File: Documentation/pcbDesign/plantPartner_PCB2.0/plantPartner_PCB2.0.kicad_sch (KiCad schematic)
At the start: 67 parts, among them IC1 MPM3610, J1 Conn_01x04, J10 Screw_Terminal_01x02, J11 Conn_01x02, J12 Conn_01x03, J13 Conn_01x03, J14 Conn_01x03, J16 Conn_01x04, J17 Conn_01x03, J2 Conn_01x04, J20 Conn_02x04_Top_Bottom, J21 Conn_01x04, J22 Conn_01x04, J23 Conn_01x01, J24 Conn_01x03, J25 Conn_01x03, J26 Conn_01x01, J27 Conn_01x01, J28 Conn_01x01, J29 Conn_01x02, J3 Conn_01x04, J30 Screw_Terminal_01x02, J4 Screw_Terminal, J5 Conn_01x02, J6 Barrel_Jack, J7 Screw_Terminal_01x02, J8 Conn_02x04_Top_Bottom, J9 Screw_Terminal_01x02, Q1 AO3400A, Q2 AO3400A, Q4 AO3400A, U2 MAX485, U3 ESP32-DEVKIT-V1

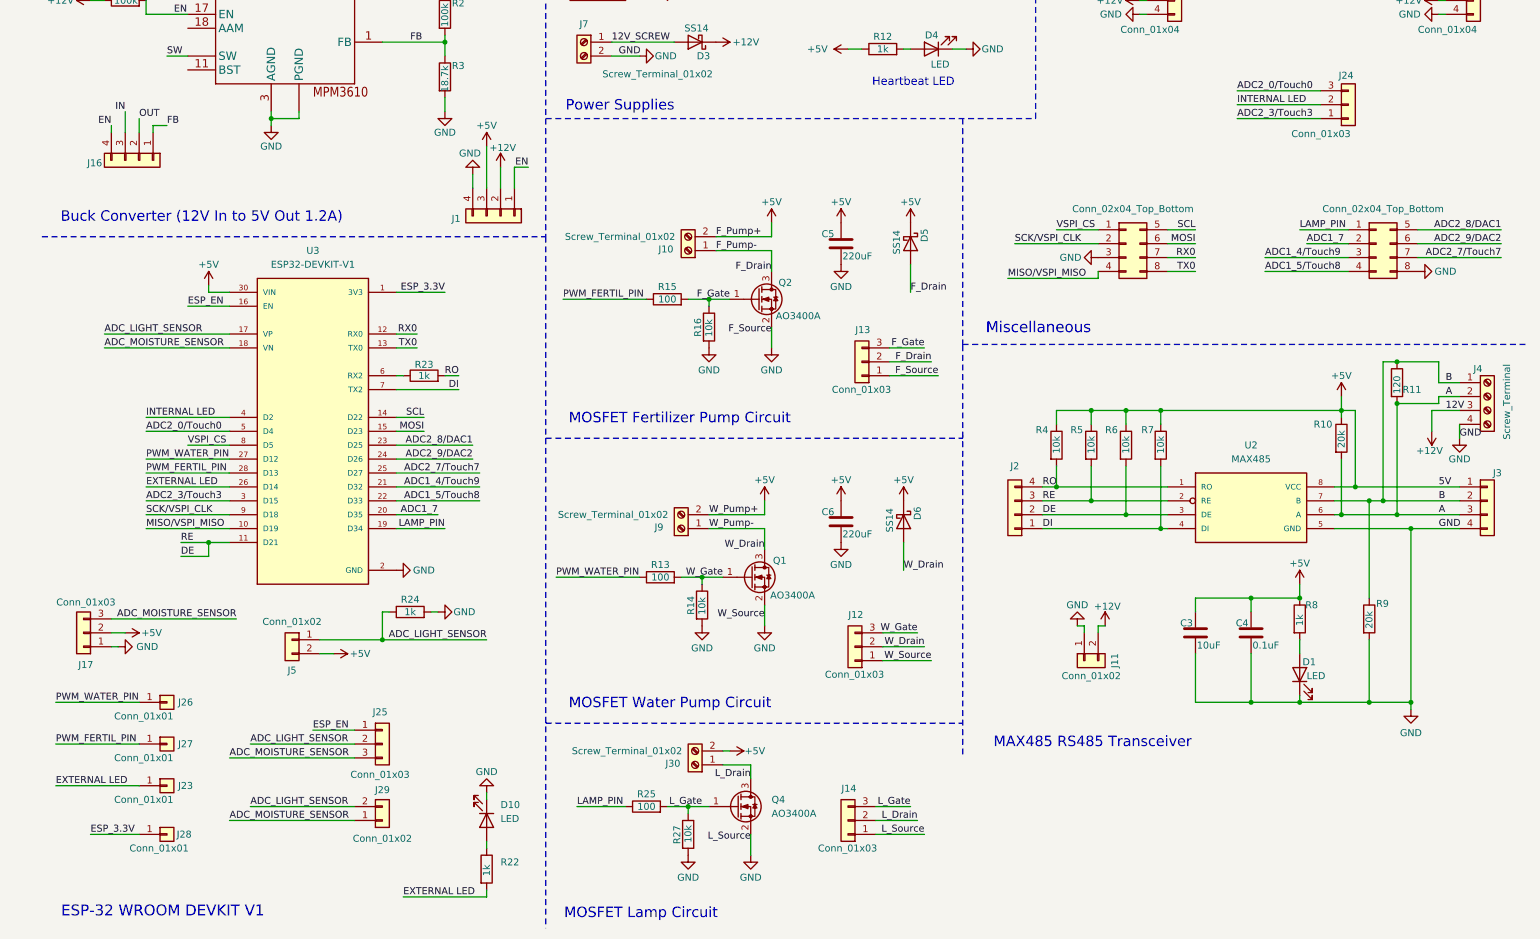
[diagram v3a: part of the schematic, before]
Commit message: Routed v2 PCB some more. Finished routing power sources, Buck Converter, MOSFET circuits, and most of RS485 Transceiver. I forgot about KiCad but will not next time I get a big chunk of time
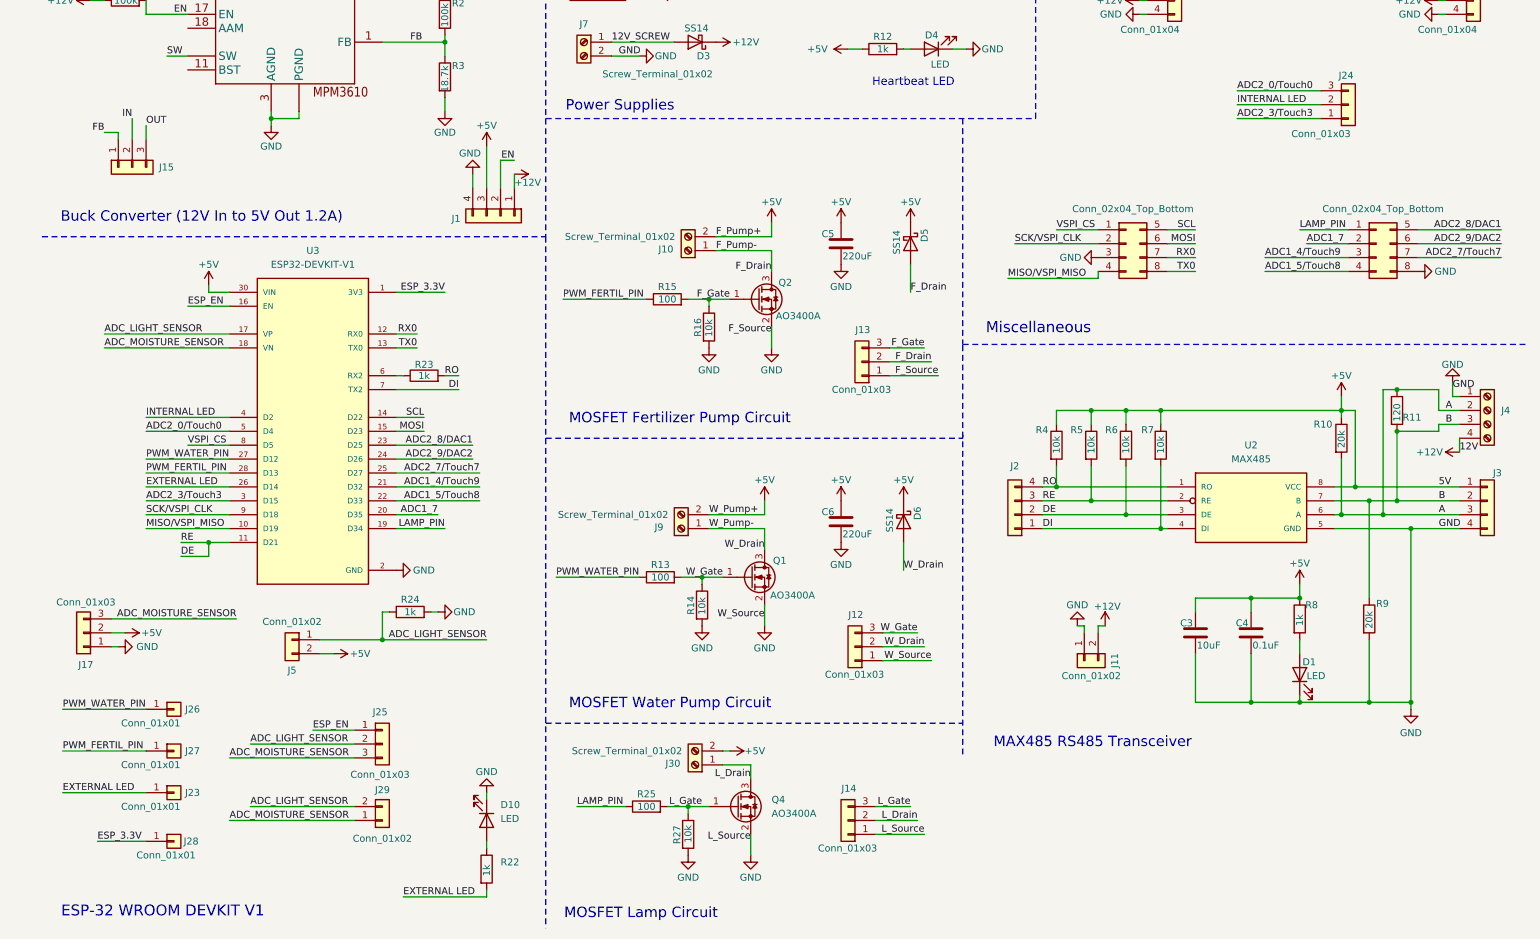
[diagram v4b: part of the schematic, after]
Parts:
- removed J16: Conn_01x04, Connector_PinHeader_2.54mm:PinHeader_1x04_P2.54mm_Vertical, symbol Connector_Generic:Conn_01x04
- added J15: Conn_01x03, Connector_PinHeader_2.54mm:PinHeader_1x03_P2.54mm_Vertical, symbol Connector_Generic:Conn_01x03
- J4: value Screw_Terminal -> Screw_Terminal_01x04
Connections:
- net +12V: now also J1.1 (Pin_1), J4.4 (Pin_4), J15.2 (Pin_2); no longer J1.2 (Pin_2), J4.3 (Pin_3)
- net +5V: now also J15.3 (Pin_3)
- net A: now also R11.1; no longer R11.2
- net B: now also J4.3 (Pin_3), R11.2; no longer J4.1 (Pin_1), R11.1
- net EN: now also J1.2 (Pin_2); no longer J1.1 (Pin_1)
- net FB: now also J15.1 (Pin_1)
- net GND: now also J4.1 (Pin_1); no longer J4.4 (Pin_4)
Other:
- moved on the sheet: J23, J26, J27, J28, R11

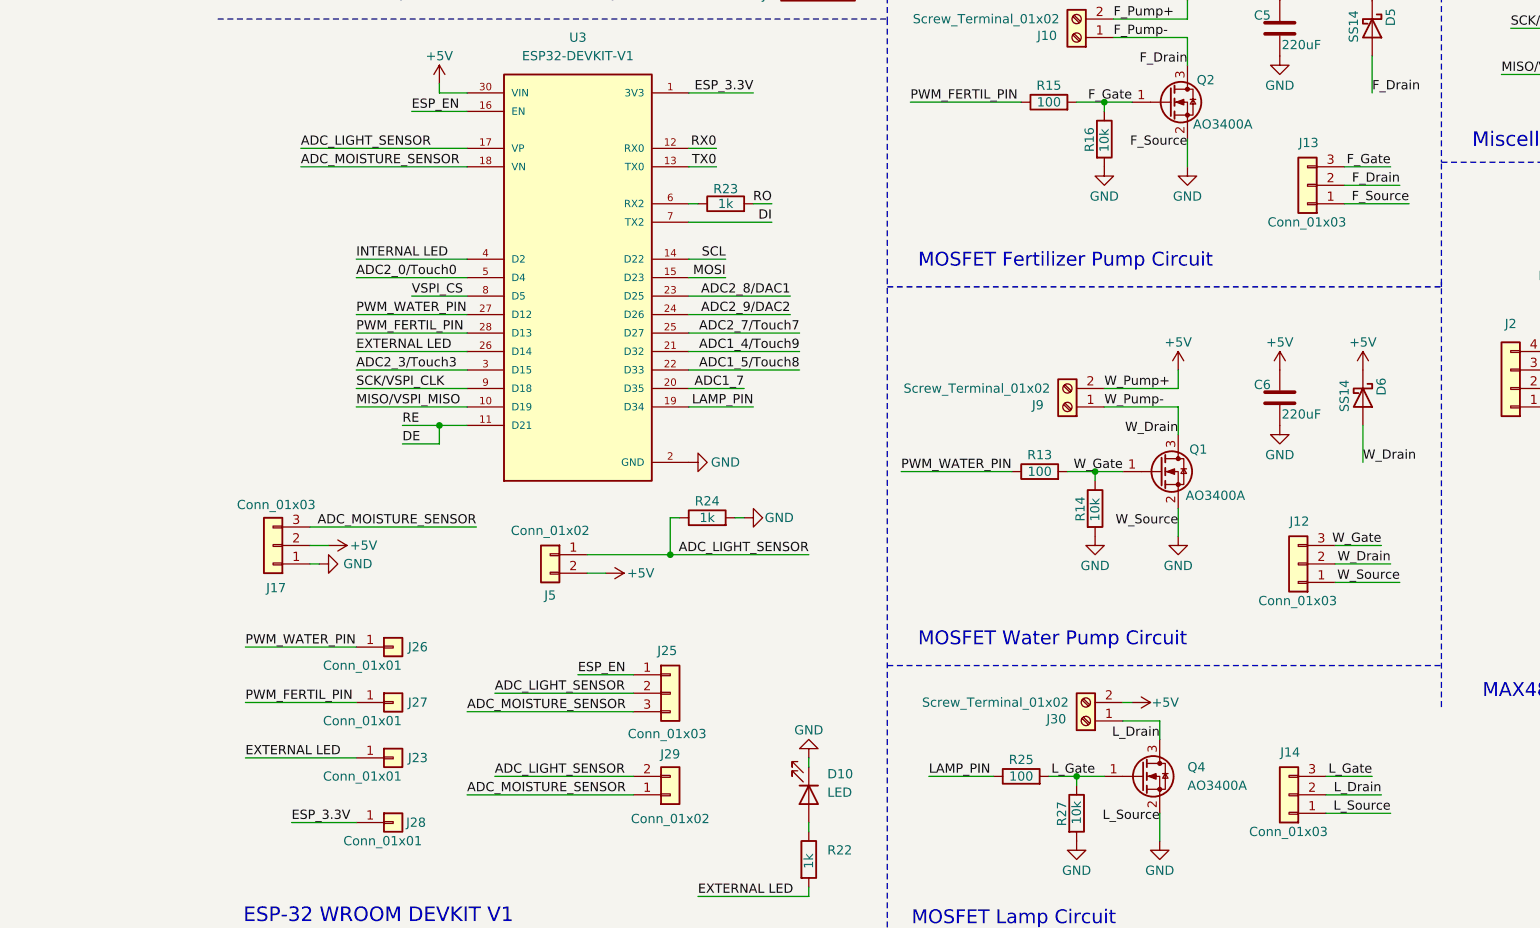
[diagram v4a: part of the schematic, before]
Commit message: Meeting with Tyler. Fully finished routing MOSFET circuits, RS485 Transceiver, and some of ADC circuits. Still need to test MOSFET circuits in Ltspice, but placed most of overall PCB into a small edge cut square that is 2.5”x2.5” which is 50% smaller and cheaper.
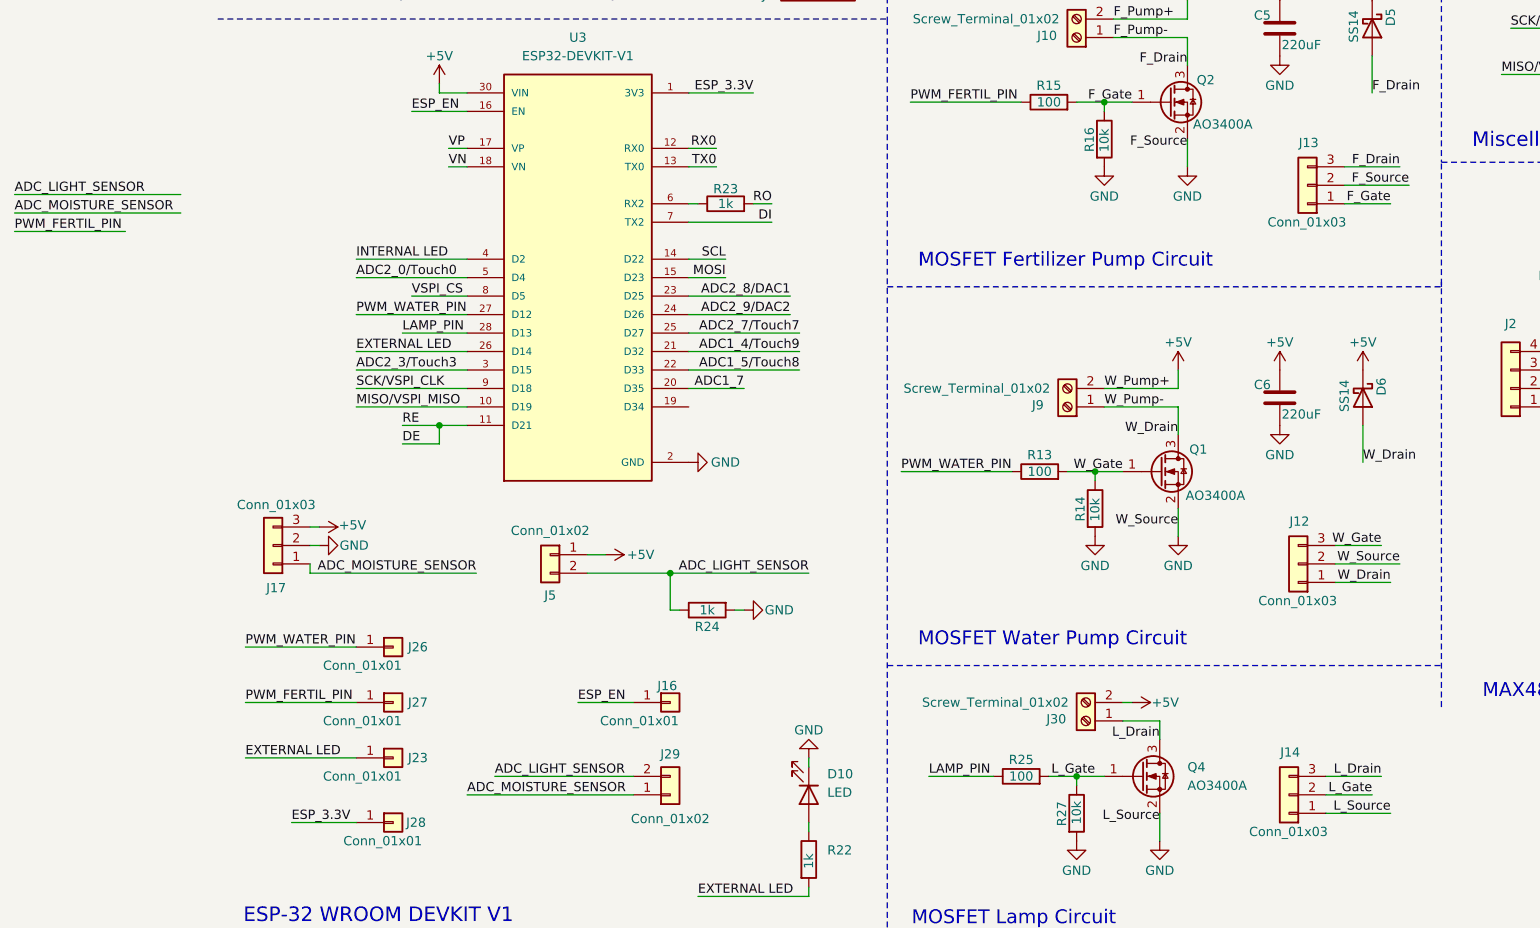
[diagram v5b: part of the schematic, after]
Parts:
- removed J25: Conn_01x03, Connector_PinHeader_2.54mm:PinHeader_1x03_P2.54mm_Vertical, symbol Connector_Generic:Conn_01x03
- added J16: Conn_01x01, Connector_PinHeader_2.54mm:PinHeader_1x01_P2.54mm_Vertical, symbol Connector_Generic:Conn_01x01
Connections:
- net +5V: now also J17.3 (Pin_3), J5.1 (Pin_1); no longer J17.2 (Pin_2), J5.2 (Pin_2)
- net ADC_LIGHT_SENSOR: now also J5.2 (Pin_2); no longer J5.1 (Pin_1), U3.17 (VP)
- net ADC_MOISTURE_SENSOR: now also J17.1 (Pin_1); no longer J17.3 (Pin_3), U3.18 (VN)
- net ESP_EN: now also J16.1 (Pin_1)
- net F_Drain: now also J13.3 (Pin_3); no longer J13.2 (Pin_2)
- net F_Gate: now also J13.1 (Pin_1); no longer J13.3 (Pin_3)
- net GND: now also J12.2 (Pin_2), J13.2 (Pin_2), J17.2 (Pin_2); no longer J12.1 (Pin_1), J13.1 (Pin_1), J17.1 (Pin_1)
- net LAMP_PIN: now also U3.28 (D13); no longer U3.19 (D34)
- net L_Drain: now also J14.3 (Pin_3); no longer J14.2 (Pin_2)
- net L_Gate: now also J14.2 (Pin_2); no longer J14.3 (Pin_3)
- net PWM_FERTIL_PIN: no longer U3.28 (D13)
- net W_Drain: now also J12.1 (Pin_1); no longer J12.2 (Pin_2)
- new net VN: U3.18 (VN)
- new net VP: U3.17 (VP)
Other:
- moved on the sheet: R24
